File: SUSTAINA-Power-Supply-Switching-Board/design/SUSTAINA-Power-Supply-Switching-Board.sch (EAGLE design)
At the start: 50 parts, among them IC1 LTC4418IUF, M1 POWER-MONITOR-MODULE, M2 POWER-MONITOR-MODULE, U1 SI7997DP-T1-GE3, U2 SI7997DP-T1-GE3

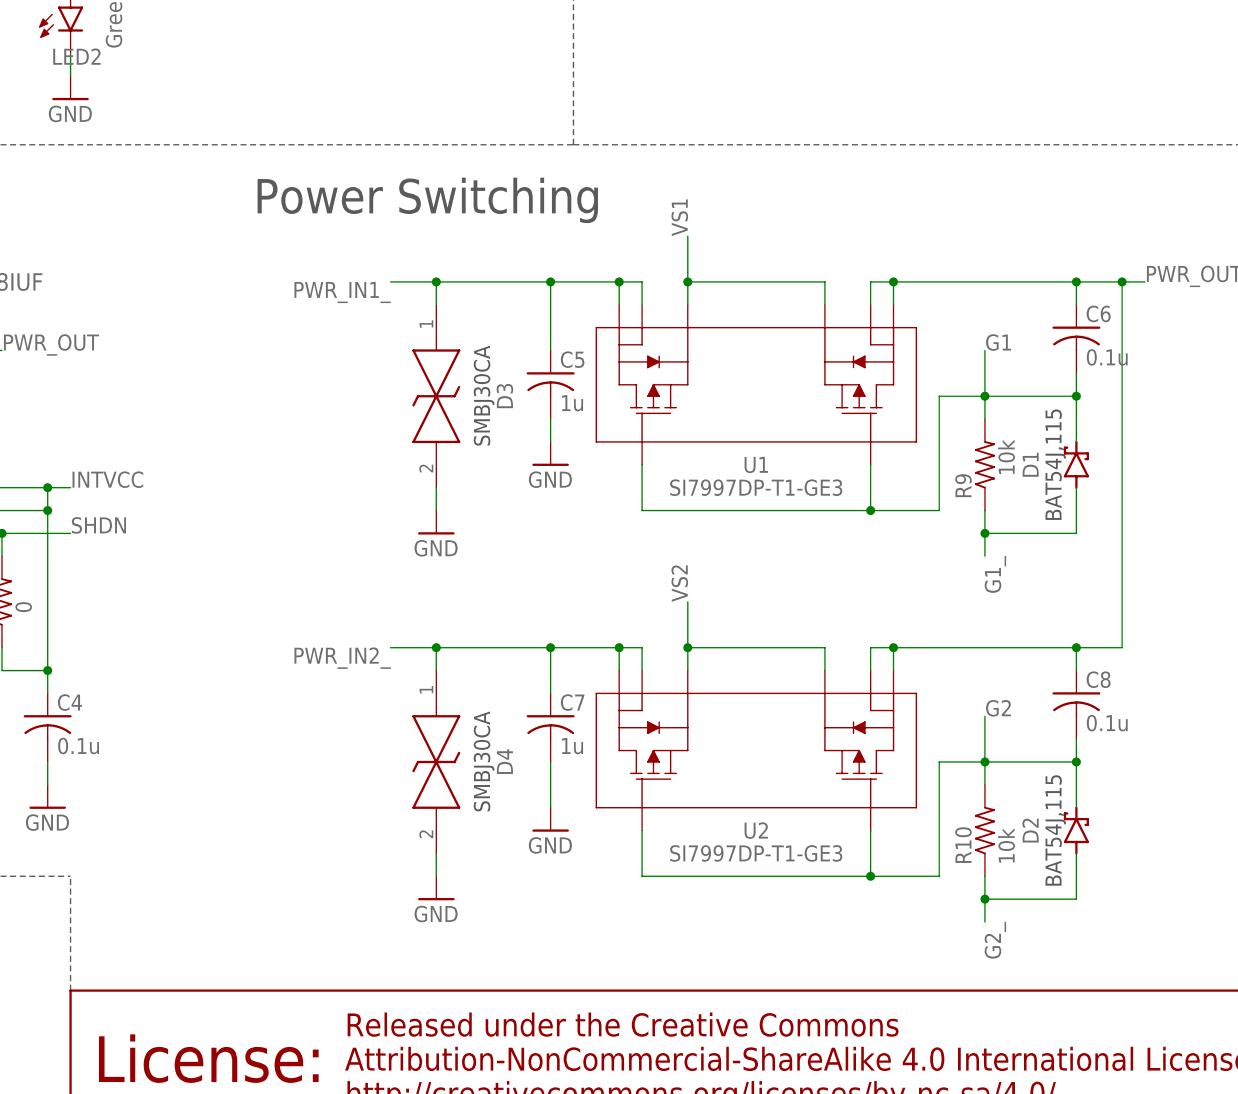
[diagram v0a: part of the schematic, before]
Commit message: Corrected a via error and added some capacitors
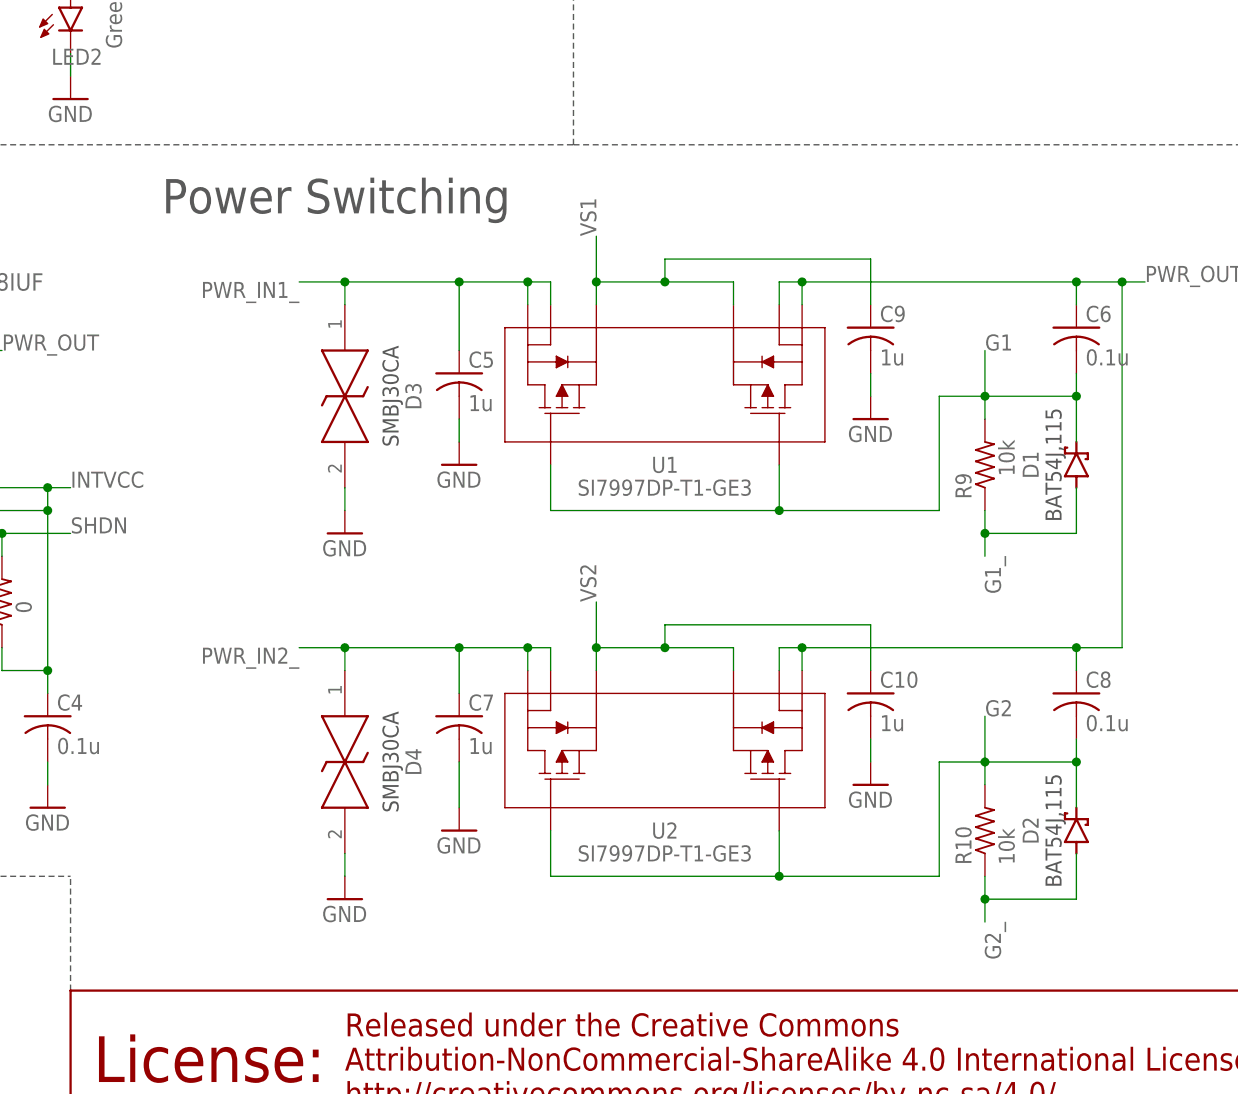
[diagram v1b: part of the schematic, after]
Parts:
- added C10, C9: 1u, rcl:C-USC0603
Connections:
- net GND: now also C10.2, C9.2
- net VS1: now also C9.1
- net VS2: now also C10.1
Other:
- moved on the sheet: C5, C7, D3, D4, U1, U2
